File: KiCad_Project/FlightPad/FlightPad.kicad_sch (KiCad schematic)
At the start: 19 parts, among them SW10 SW_Push, SW2 SW_Push, SW3 SW_Push, SW4 SW_Push, SW5 SW_Push, SW6 SW_Push, SW7 SW_Push, SW8 SW_Push, SW9 SW_Push, U1 XIAO-RP2040-DIP

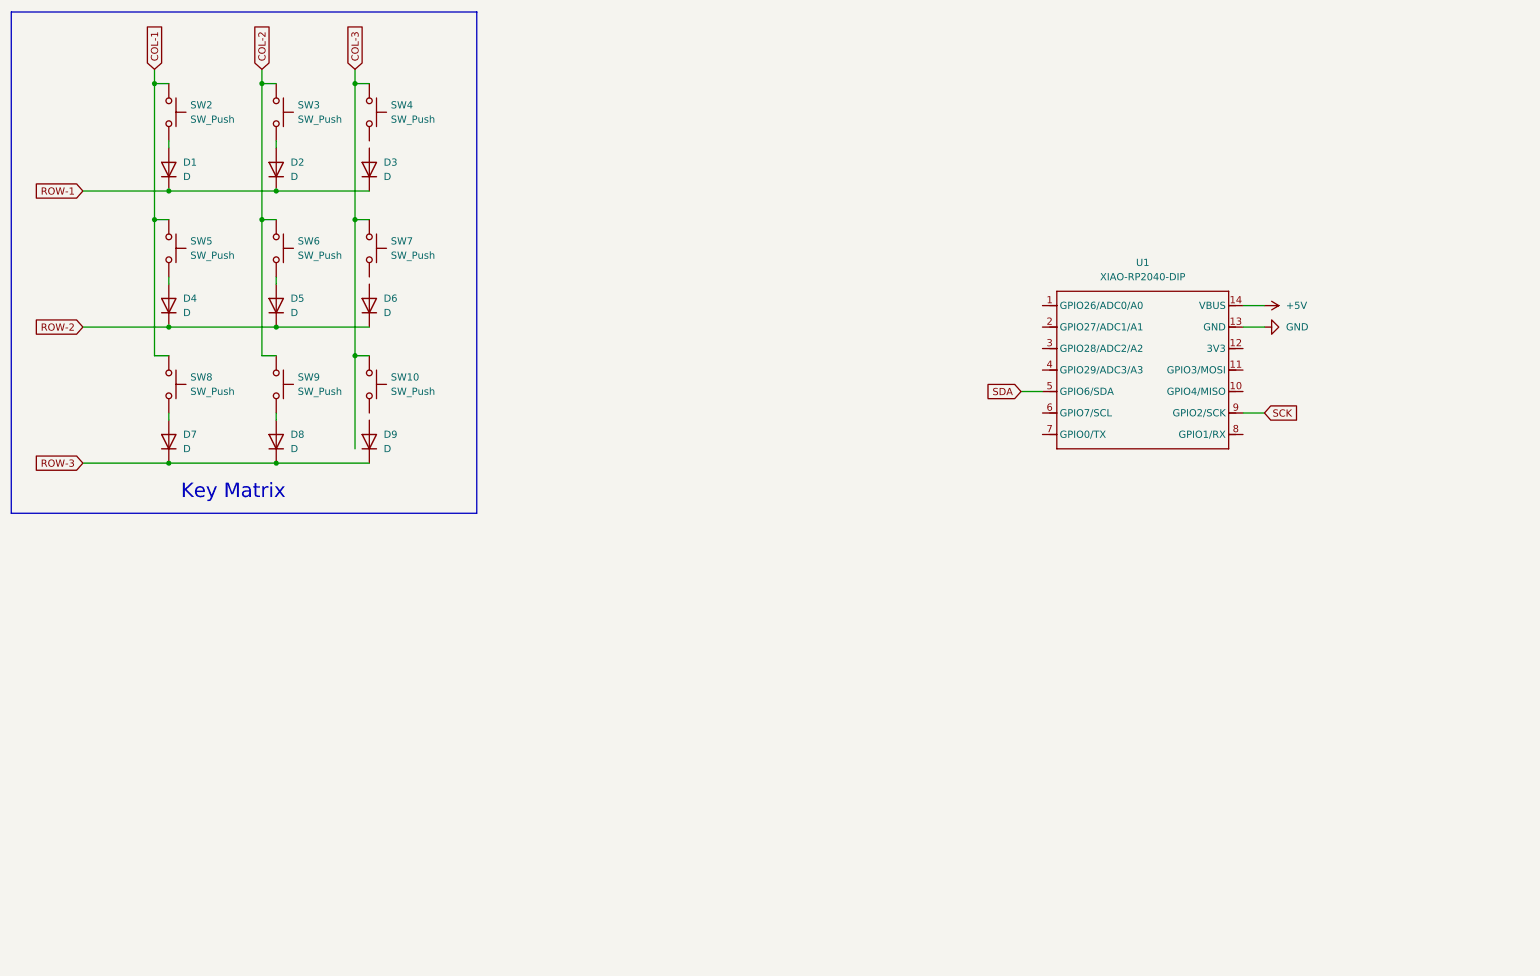
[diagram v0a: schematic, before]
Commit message: Added the Oled display.  Tidied up the schematic. added a description
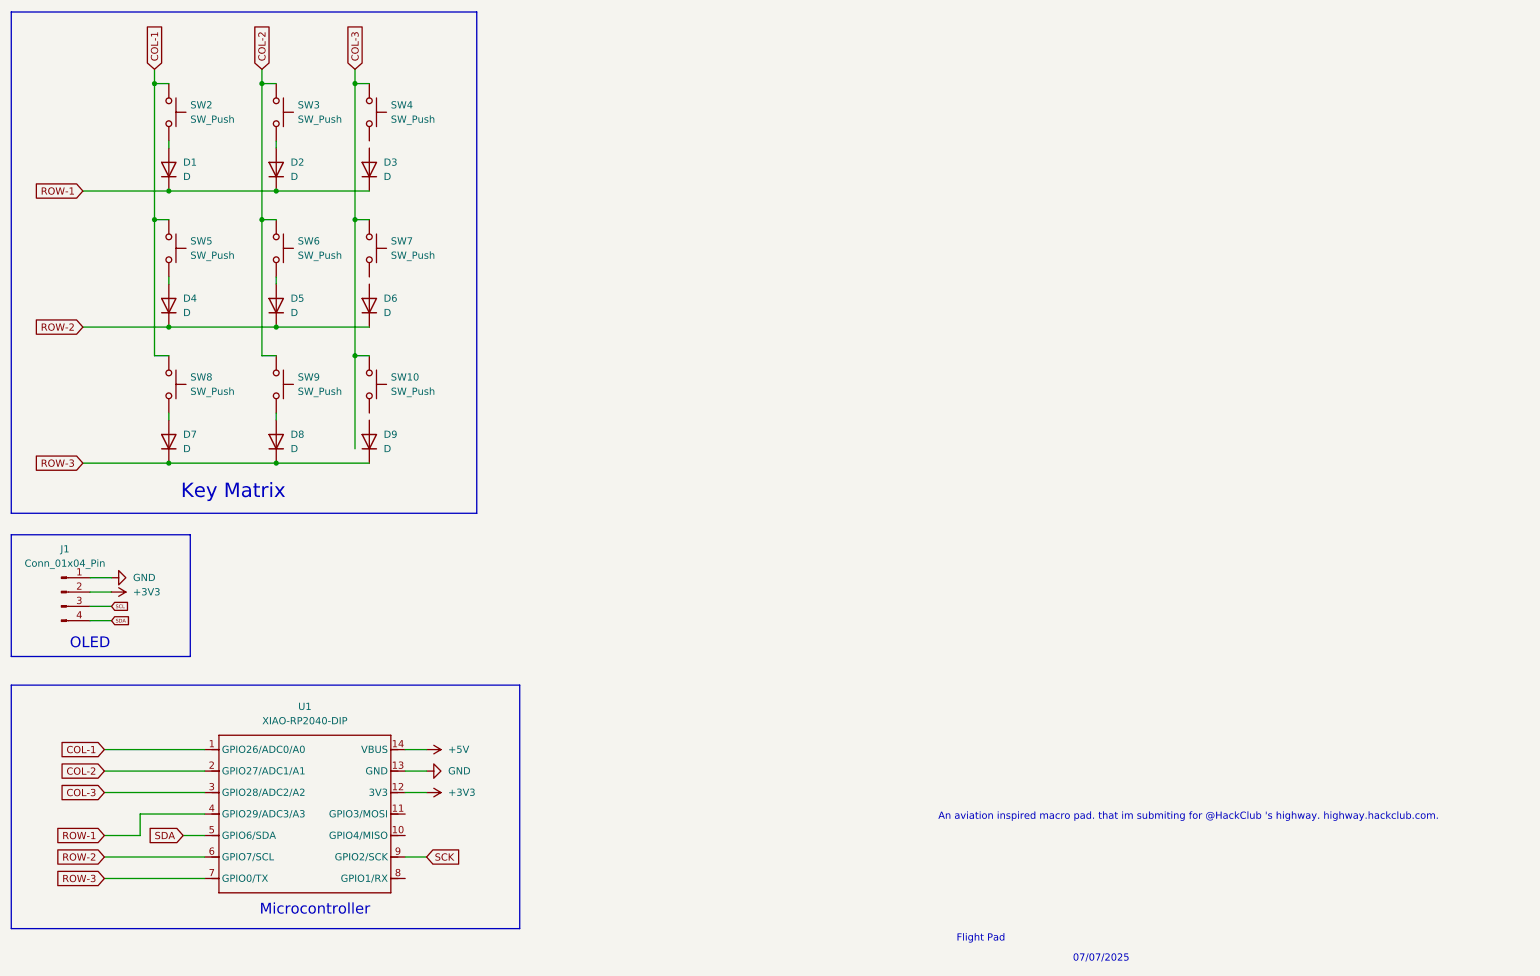
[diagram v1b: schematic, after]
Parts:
- added J1: Conn_01x04_Pin, symbol Connector:Conn_01x04_Pin
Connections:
- net COL-1: now also U1.1 (GPIO26/ADC0/A0)
- net COL-2: now also U1.2 (GPIO27/ADC1/A1)
- net COL-3: now also U1.3 (GPIO28/ADC2/A2)
- net GND: now also J1.1 (Pin_1)
- net ROW-1: now also U1.4 (GPIO29/ADC3/A3)
- net ROW-2: now also U1.6 (GPIO7/SCL)
- net ROW-3: now also U1.7 (GPIO0/TX)
- net SDA: now also J1.4 (Pin_4)
- net +3V3: now reaches U1.12 (3V3)
- net +3V3: now also J1.2 (Pin_2)
- new net SCL: J1.3 (Pin_3)
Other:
- note added: "07/07/2025"
- note added: "An aviation inspired macro pad. that im submiting for @HackClub 's highway. highway.hackclub.com."
- note added: "Flight Pad"
- note added: "Microcontroller"
- note added: "OLED"
- moved on the sheet: U1
